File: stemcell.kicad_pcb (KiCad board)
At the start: 2 copper layers, 17.8 x 31.9 mm, 37 parts, among them J1 USB C Connector, J2 Left, J3 Right, J4 Down, SW1 Boot0, U1 STM32F4x1CxUx, U2 XC6220B331MR, Y1 HSE1 8Mhz 12pF

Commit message: Added watermark
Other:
- board text added: "Printed by devcexx"
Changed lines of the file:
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@@
 	)
 	(gr_text "@megamind4089"
-		(at 100.1268 70.866 0)
+		(at 100.1268 68.6 0)
 		(layer "B.SilkS")
 		(effects
@@
 			)
 			(justify mirror)
+		)
+	)
+	(gr_text "Printed by devcexx"
+		(at 100 70.8 0)
+		(layer "B.SilkS")
+		(effects
+			(font
+				(size 0.7 0.7)
+				(thickness 0.1)
+			)
+			(justify mirror)

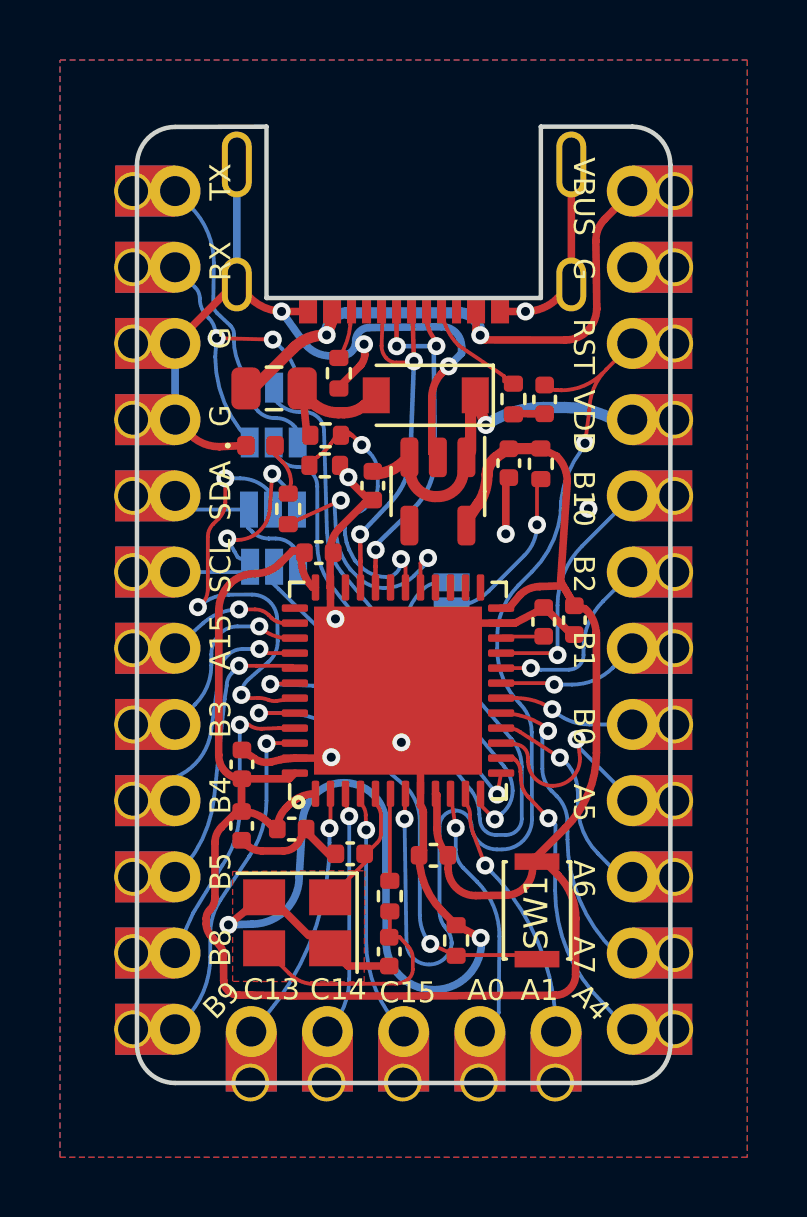
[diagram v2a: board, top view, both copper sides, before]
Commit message: Rerouted USB section to fit replacement USB connector PN C2874573
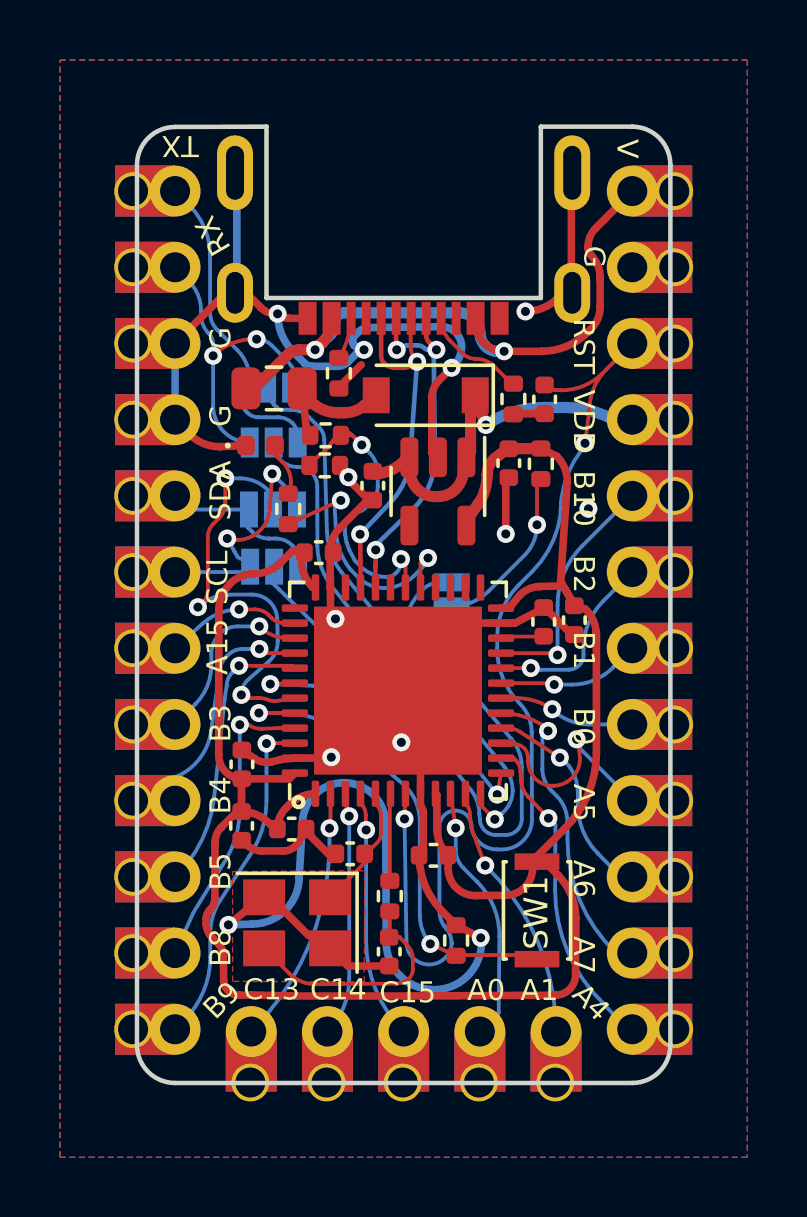
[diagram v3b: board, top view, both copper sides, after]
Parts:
- J1: footprint stemcell:USB-C-C168688 -> stemcell:USB-C-SMD_MC-109-C10
- moved J1 4.80 mm to (100.1, 53.2), turned to 180 degrees
- moved JP1 0.23 mm to (95.5, 57.9)
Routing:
- net VBUS: track 19.6 -> 22.1 mm
- net /TX0: track 10.2 -> 11.2 mm
- net /RX0: track 10.3 -> 11.0 mm
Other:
- board text added: "V"

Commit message: Re-routed USB signals
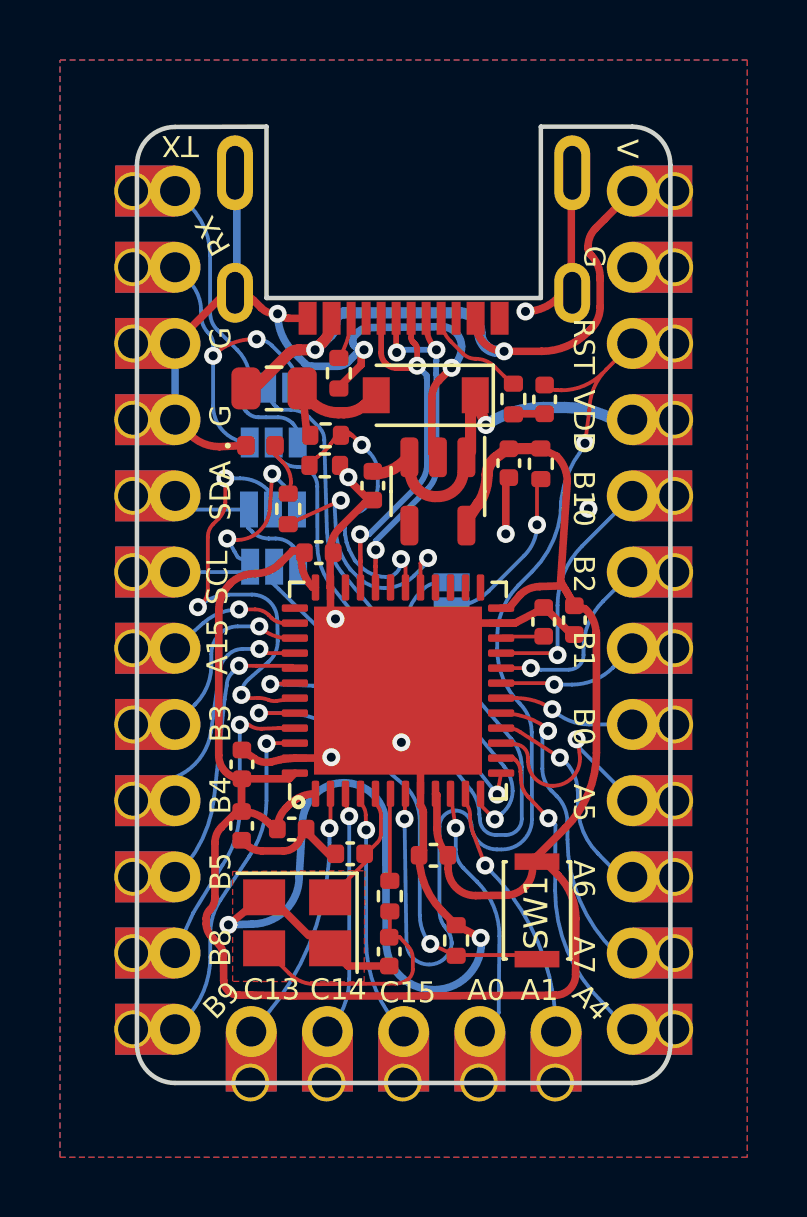
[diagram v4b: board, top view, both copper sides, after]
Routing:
- net /USB_DP: track 12.4 -> 12.9 mm

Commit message: Bumped to v2.2.0
* Removed paste from USB-C PTH holes.
* Added JLCPCB Rotations and position offsets for PCBA.
* Fixed some minor issues after reviewing it for printing.
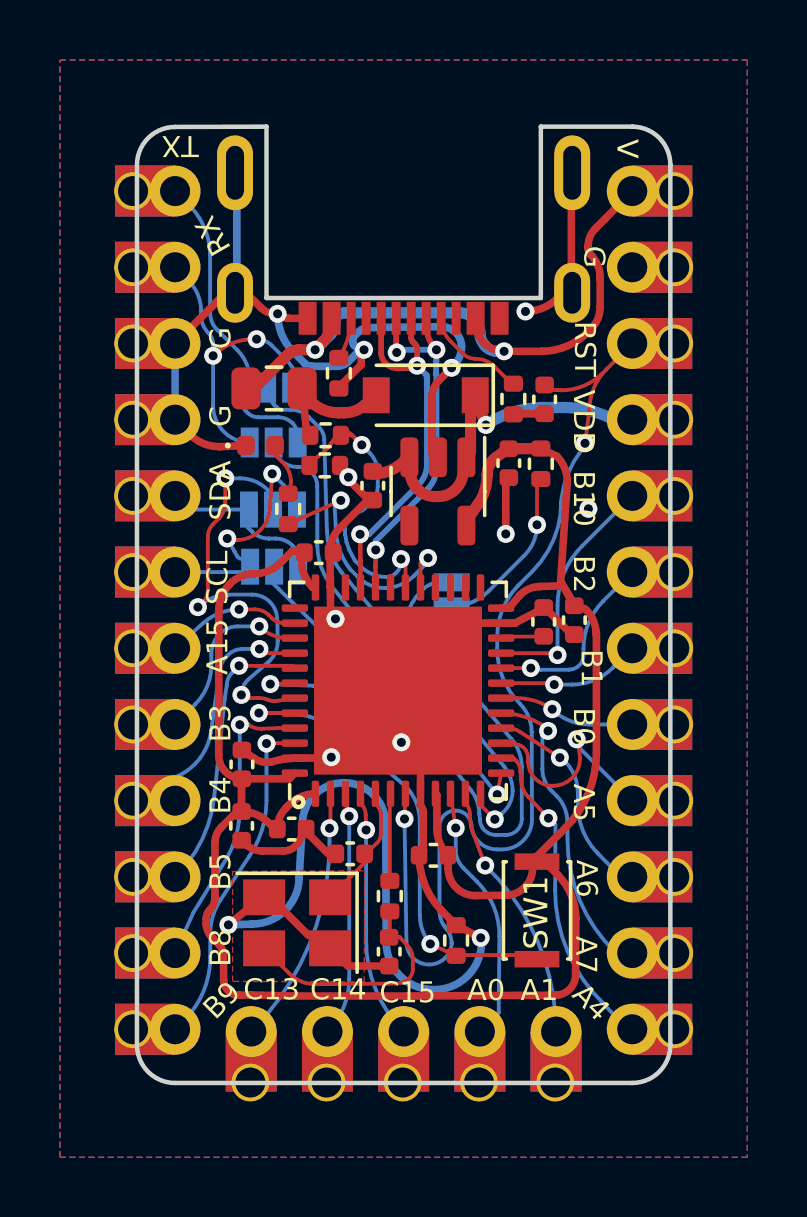
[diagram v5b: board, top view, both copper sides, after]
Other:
- board text added: "Revamp by devcexx"
- board text added: "v2.2.0"
- board text removed: "Printed by devcexx"
- board text removed: "VBUS"
- board text removed: "v2.1.0"
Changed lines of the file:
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@@
 	(title_block
 		(title "STeMCell")
-		(date "2022-08-08")
-		(rev "2.0.0")
+		(date "2025-03-02")
+		(rev "2.2.0")
 	)
 	(layers
@@
 		(property "Reference" "J1"
 			(at 0 -3.8635 180)
-			(layer "F.SilkS")
-			(hide yes)
+			(layer "F.Fab")
 			(effects
 				(font
@@
 			)
 		)
+		(property "PosOffset" "0,0.15"
+			(at 0 0 0)
+			(unlocked yes)
+			(layer "F.Fab")
+			(hide yes)
+			(effects
+				(font
+					(size 1 1)
+					(thickness 0.15)
+				)
+			)
+		)
 		(sheetfile "stemcell.kicad_sch")
 		(fp_poly
@@
 			(layer "F.Paste")
 		)
-		(fp_poly
-			(pts
-				(arc
-					(start 5.02 1.775)
-					(mid 5.62 1.175)
-					(end 6.22 1.775)
-				)
-				(arc
-					(start 6.22 3.075)
-					(mid 5.62 3.675)
-					(end 5.02 3.075)
-				)
-			)
-			(stroke
-				(width 0)
-				(type default)
-			)
-			(fill yes)
-			(layer "F.Paste")
-		)
-		(fp_poly
-			(pts
-				(arc
-					(start 5.02 -1.975)
-					(mid 5.62 -2.575)
-					(end 6.22 -1.975)
-				)
-				(arc
-					(start 6.22 -1.175)
-					(mid 5.62 -0.575)
-					(end 5.02 -1.175)
-				)
-			)
-			(stroke
-				(width 0)
-				(type default)
-			)
-			(fill yes)
-			(layer "F.Paste")
-		)
-		(fp_poly
-			(pts
-				(arc
-					(start -6.22 1.775)
-					(mid -5.62 1.175)
-					(end -5.02 1.775)
-				)
-				(arc
-					(start -5.02 3.075)
-					(mid -5.62 3.675)
-					(end -6.22 3.075)
-				)
-			)
-			(stroke
-				(width 0)
-				(type default)
-			)
-			(fill yes)
-			(layer "F.Paste")
-		)
-		(fp_poly
-			(pts
-				(arc
-					(start -6.22 -1.975)
-					(mid -5.62 -2.575)
-					(end -5.02 -1.975)
-				)
-				(arc
-					(start -5.02 -1.175)
-					(mid -5.62 -0.575)
-					(end -6.22 -1.175)
-				)
-			)
-			(stroke
-				(width 0)
-				(type default)
-			)
-			(fill yes)
-			(layer "F.Paste")
-		)
 		(fp_line
 			(start 4.53 1.369)
@@
 		(tags "SOT TO_SOT_SMD")
 		(property "Reference" "U2"
-			(at -1.2751 0.1636 180)
+			(at -1.2751 0.1636 0)
 			(layer "User.8")
 			(effects
@@
 		)
 		(property "Datasheet" ""
-			(at 0 0 270)
+			(at 0 0 90)
 			(layer "F.Fab")
 			(hide yes)
@@
 		)
 		(property "Description" ""
-			(at 0 0 270)
+			(at 0 0 90)
 			(layer "F.Fab")
 			(hide yes)
@@
 			)
 		)
+		(property "RotOffset" "180"
+			(at 0 0 0)
+			(unlocked yes)
+			(layer "F.Fab")
+			(hide yes)
+			(effects
+				(font
+					(size 1 1)
+					(thickness 0.15)
+				)
+			)
+		)
 		(sheetfile "stemcell.kicad_sch")
 		(attr smd)
@@
 			)
 		)
+		(property "RotOffset" "180"
+			(at 0 0 0)
+			(unlocked yes)
+			(layer "F.Fab")
+			(hide yes)
+			(effects
+				(font
+					(size 1 1)
+					(thickness 0.15)
+				)
+			)
+		)
 		(sheetfile "stemcell.kicad_sch")
 		(attr smd)
@@
 			)
 		)
+		(property "RotOffset" "180"
+			(at 0 0 0)
+			(unlocked yes)
+			(layer "F.Fab")
+			(hide yes)
+			(effects
+				(font
+					(size 1 1)
+					(thickness 0.15)
+				)
+			)
+		)
 		(sheetfile "stemcell.kicad_sch")
 		(attr smd)
@@
 			)
 		)
+		(model "${KICAD9_3DMODEL_DIR}/Package_DFN_QFN.3dshapes/QFN-48-1EP_7x7mm_P0.5mm_EP5.15x5.15mm.wrl"
+			(offset
+				(xyz 0 0 0)
+			)
+			(scale
+				(xyz 1 1 1)
+			)
+			(rotate
+				(xyz 0 0 0)
+			)
+		)
 	)
 	(footprint "Resistor_SMD:R_0402_1005Metric"
@@
 		)
 		(property "Datasheet" ""
-			(at 0 0 270)
+			(at 0 0 90)
 			(layer "F.Fab")
 			(hide yes)
@@
 		)
 		(property "Description" ""
-			(at 0 0 270)
+			(at 0 0 90)
 			(layer "F.Fab")
 			(hide yes)
@@
 		)
 		(sheetfile "stemcell.kicad_sch")
-		(attr exclude_from_pos_files)
+		(attr exclude_from_pos_files exclude_from_bom)
 		(pad "1" smd rect
 			(at -0.8 0 270)
@@
 		)
 		(sheetfile "stemcell.kicad_sch")
-		(attr exclude_from_pos_files)
+		(attr exclude_from_pos_files exclude_from_bom)
 		(pad "1" smd rect
 			(at -0.8 0 180)
@@
 		)
 		(sheetfile "stemcell.kicad_sch")
-		(attr exclude_from_pos_files)
+		(attr exclude_from_pos_files exclude_from_bom)
 		(pad "1" smd rect
 			(at -0.8 0 180)
@@
 		)
 		(sheetfile "stemcell.kicad_sch")
-		(attr exclude_from_pos_files)
+		(attr exclude_from_pos_files exclude_from_bom)
 		(pad "1" smd rect
 			(at -0.8 0)
@@
 		)
 		(sheetfile "stemcell.kicad_sch")
-		(attr exclude_from_pos_files)
+		(attr exclude_from_pos_files exclude_from_bom)
 		(pad "1" smd rect
 			(at -0.8 0)
@@
 	)
 	(gr_text "RST"
-		(at 106.1024 56.5308 -90)
+		(at 106.14 56.62 -90)
 		(layer "F.SilkS")
 		(effects
@@
 	)
 	(gr_text "B1"
-		(at 106.1024 66.6654 -90)
+		(at 106.36 67.26 -90)
 		(layer "F.SilkS")
 		(effects
@@
 	)
 	(gr_text "A6"
-		(at 106.1024 74.2854 -90)
+		(at 106.2 74.28 -90)
 		(layer "F.SilkS")
 		(effects
@@
 	)
 	(gr_text "A7"
-		(at 106.1024 76.8254 -90)
+		(at 106.18 76.82 -90)
 		(layer "F.SilkS")
 		(effects
@@
 		)
 	)
-	(gr_text "v2.1.0"
+	(gr_text "v2.2.0"
 		(at 97.2 76.575 0)
 		(layer "B.SilkS")
@@
 	)
 	(gr_text "RX"
-		(at 93.988719 53.81 90)
+		(at 93.67 52.85 120)
 		(layer "B.SilkS")
 		(effects
@@
 	)
 	(gr_text "TX"
-		(at 93.988719 51.1684 90)
+		(at 92.54 49.82 180)
 		(layer "B.SilkS")
 		(effects
@@
 	)
 	(gr_text "G"
-		(at 106.1 53.97 270)
+		(at 106.43 53.62 270)
 		(layer "B.SilkS")
 		(effects
@@
 		)
 	)
-	(gr_text "VBUS"
-		(at 106.1 51.5454 270)
+	(gr_text "V"
+		(at 107.57 49.96 270)
 		(layer "B.SilkS")
 		(effects
@@
 		)
 	)
-	(gr_text "Printed by devcexx"
+	(gr_text "Revamp by devcexx"
 		(at 100 70.8 0)
 		(layer "B.SilkS")
@@
 		)
 	)
-	(group "Left F.Silk"
-		(members "263e9b7e-c3cd-4442-851e-d2b54de99d8e" "36cd765a-f621-46fc-9b88-d90e333169eb"
-			"50804f87-f832-4c63-a5a7-b7f94bf6665d" "75f01a69-5b72-43de-ae85-3f0e1d096e8d"
-			"79a5a253-5ade-4145-9002-16ea61146340" "95ef25aa-dac6-44d9-90a0-efd49308b704"
-			"b29a0e42-fd5a-49a8-8a01-edc4123e673b" "b8dbe2de-283b-405e-95ac-e8f8950e16ea"
-			"bc96b171-0e5f-4f36-b582-eb709cbba257" "cb61a608-4d4c-465e-98f1-04dc591a70ac"
-			"dd9691e0-5bea-4f21-9741-4d29638cd32d" "e226f21d-d833-4b38-a2cd-20826072ac2f"
-		)
-	)
 	(group "Down F. Silk"
 		(members "076ec102-1264-42f9-b892-abc9c2acc57a" "3dadfe80-aa2c-4ebe-90f6-b3b281c7c270"
@@
 		(members "62e581dc-1e92-48f0-ba03-062cdbe9f1af" "80338cc4-846d-46da-911e-25dfdc54c17a")
 	)
-	(group "Right F.Silk"
-		(members "0ea296d6-5875-4618-860c-bfe68796f5b4" "236eb5d3-1a80-4626-bf3d-45645c8c1c5e"
-			"43b4c41e-2f8b-4ca3-9572-a148323b8957" "721eced1-7601-448b-b032-57ae840a5bc6"
-			"7cd8109f-5f99-46a5-9e32-14f7754144db" "811381f4-772f-4b0d-8bef-e02e7a34c83e"
-			"86bb7e54-f037-47a0-b596-e108d6b4f269" "b576af53-9779-4b42-bea4-4d91783d8c4b"
-			"b9a616d4-042f-40dd-b821-3bd00708dff1" "bb30a1ab-4552-453e-850d-50bc465e6071"
-			"c0eebf2a-4881-44d5-83b5-dc6c113fd0d3" "d3bd2f73-786f-472c-89b7-10fd054df22c"
-		)
-	)
 	(embedded_fonts no)
